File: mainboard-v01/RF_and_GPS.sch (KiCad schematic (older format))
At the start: 12 parts, among them U12 EP2W+, U13 RFM23BP, U14 S1216V8, U15 XTB_2018_07_15, U16 XTB_2018_07_15, U17 XTB_2018_07_15, U18 XTB_2018_07_15, X1 BU-SMA-V, X2 BU-SMA-V, X3 BU-SMA-V

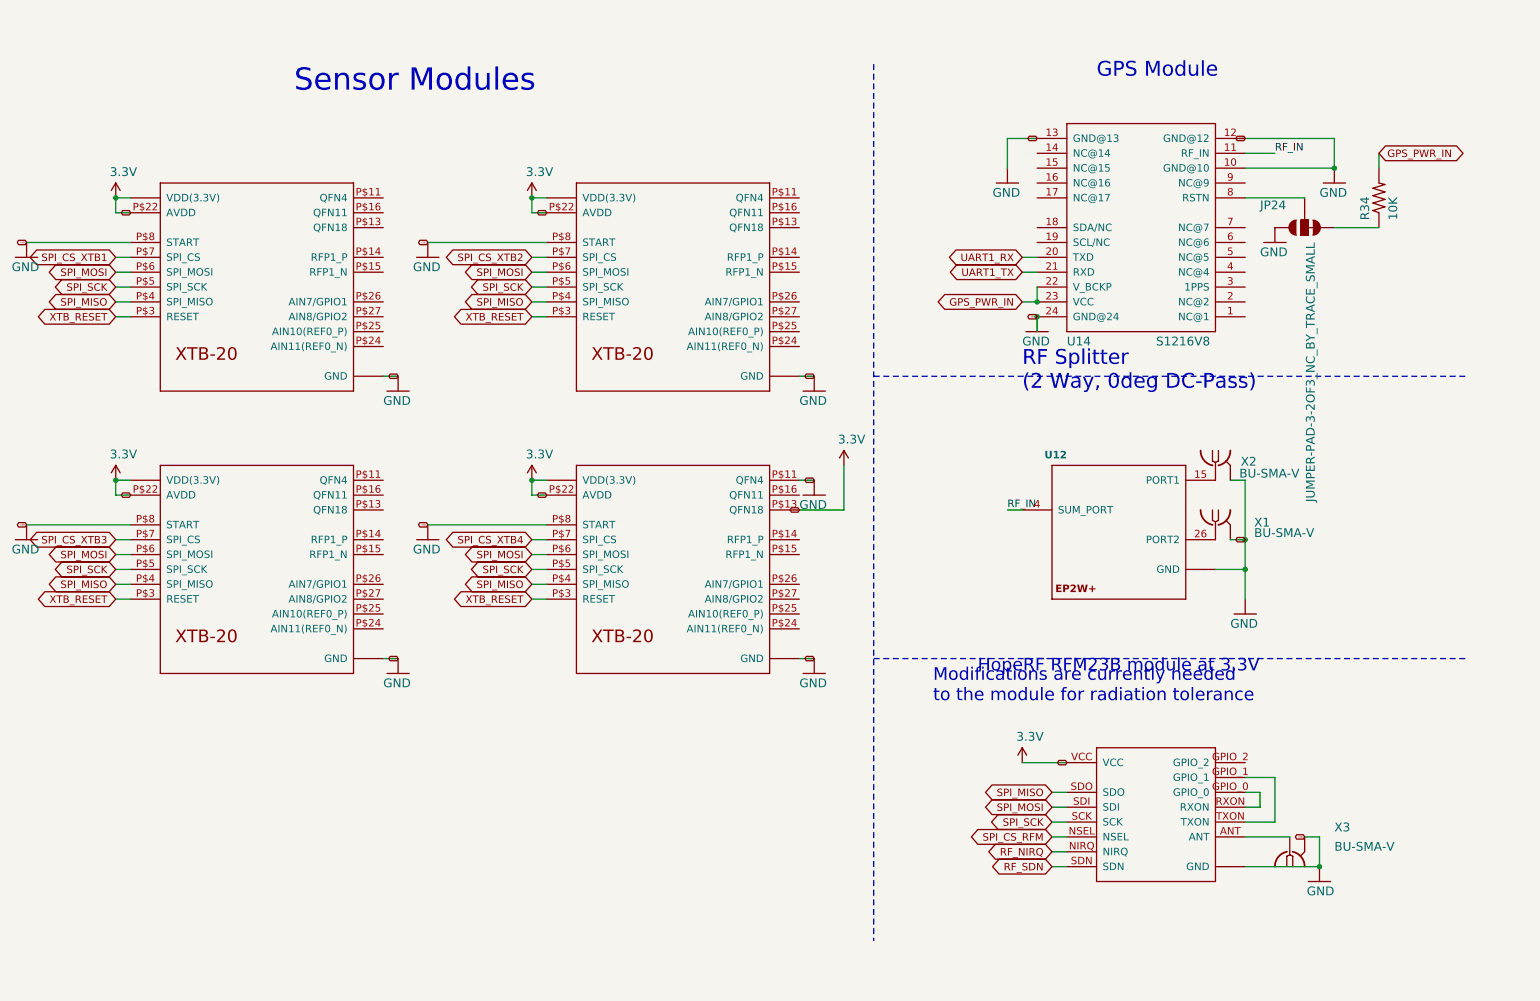
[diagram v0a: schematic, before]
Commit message: adding v01 schematic pdf
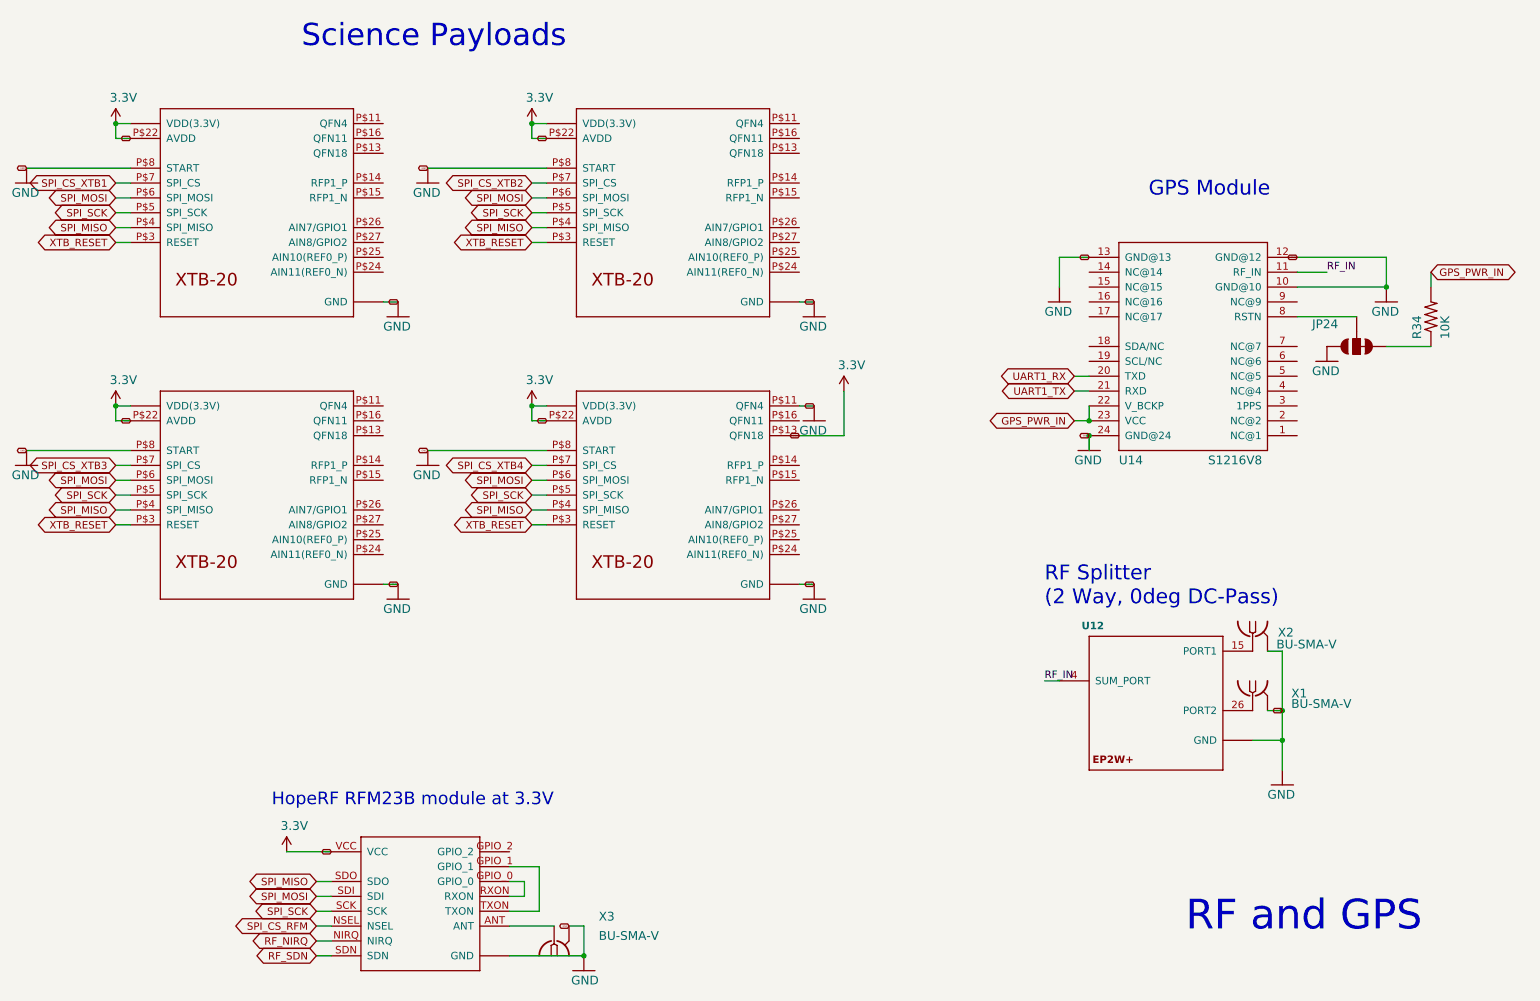
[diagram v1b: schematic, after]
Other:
- note added: "RF and GPS"
- note added: "Science Payloads"
- note removed: "Modifications are currently needed\nto the module for radiation tolerance"
- note removed: "Sensor Modules"
- moved on the sheet: JP24, R34, U12, U14, X1, X2, X3
